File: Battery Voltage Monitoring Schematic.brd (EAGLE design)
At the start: 82.2 x 68.6 mm, 44 parts, among them IC1 74HC595D, J1 22-27-2031-03, U1 INA3221., U2 INA3221., X1 22-27-2021-02, X3 2516-

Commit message: Add files via upload
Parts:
- removed PAD10_M1, PAD11_GND, PAD12_M2, PAD13_GND, PAD14_M3, PAD15_GND, PAD16_M4, PAD1_GND, PAD2_B1, PAD3_GND, PAD4_B2, PAD5_GND, PAD6_B3, PAD7_GND, PAD8_B4, PAD9_GND: 3,81/1,9, Moira:3,81/1,9
- removed X1: 22-27-2021-02, con-molex:6410-02
- added U$1, U$2, U$3, U$4, U$5, U$6, U$7, U$8: MKDS_5/2-6,352, Moira:MKDS_5/2-6,35
- added U$10: ARVP_LOGO, ARVP:ARVP
- added U$9: ARVP_MOLEX_FEMALE, ARVP_MOLEX_FEMALE:ARVP_MOLEX_FEMALE
- moved R4 40.9 mm to (36.8, 74.9), turned to 180 degrees
- moved R7 25.9 mm to (36.8, 36.8), turned to 180 degrees
- moved R1 21.7 mm to (36.8, 62.2), turned to 180 degrees
- moved R3 11.7 mm to (36.8, 49.5), turned to 180 degrees
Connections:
- net +5V: now also U$9.P$1; no longer X1.1
- net 0-26V_BATTERY1: now also U$1.1; no longer PAD2_B1.1
- net 0-26V_BATTERY2: now also U$2.1; no longer PAD4_B2.1
- net 0-26V_BATTERY3: now also U$3.1; no longer PAD6_B3.1
- net 0-26V_BATTERY4: now also U$4.1; no longer PAD8_B4.1
- net AGND: now also U$1.2, U$2.2, U$3.2, U$4.2, U$5.2, U$6.2, U$7.2, U$8.2; no longer PAD11_GND.1, PAD13_GND.1, PAD15_GND.1, PAD1_GND.1, PAD3_GND.1, PAD5_GND.1, PAD7_GND.1, PAD9_GND.1
- net GND: now also U$9.P$2; no longer X1.2
- net MOTOR1: now also U$5.1; no longer PAD10_M1.1
- net MOTOR2: now also U$6.1; no longer PAD12_M2.1
- net MOTOR3: now also U$7.1; no longer PAD14_M3.1
- net MOTOR4: now also U$8.1; no longer PAD16_M4.1
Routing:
- net 0-26V_BATTERY1: track 90.3 -> 141.5 mm, vias 2 -> 3
- net 0-26V_BATTERY3: track 96.6 -> 131.2 mm
- net 0-26V_BATTERY2: track 87.2 -> 116.2 mm, vias 0 -> 2
- net MOTOR1: track 119.1 -> 90.6 mm, vias 2 -> 1
- net MOTOR2: track 103.5 -> 87.2 mm, vias 4 -> 3
- net AGND: track 46.6 -> 32.3 mm
- net 0-26V_BATTERY4: track 90.6 -> 100.4 mm
- net MOTOR3: track 86.0 -> 78.7 mm, vias 1 -> 0
- net MOTOR4: track 62.8 -> 69.2 mm, vias 3 -> 2
- net +5V: track 74.6 -> 70.9 mm
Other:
- board size 82.2 x 68.6 mm -> 82.2 x 88.9 mm
- board text added: "ARVP BATTERY VOLTAGE MONITORING"
- board text added: "M. Blenkinsopp"
- board text added: "REV 1.1 07/2017"

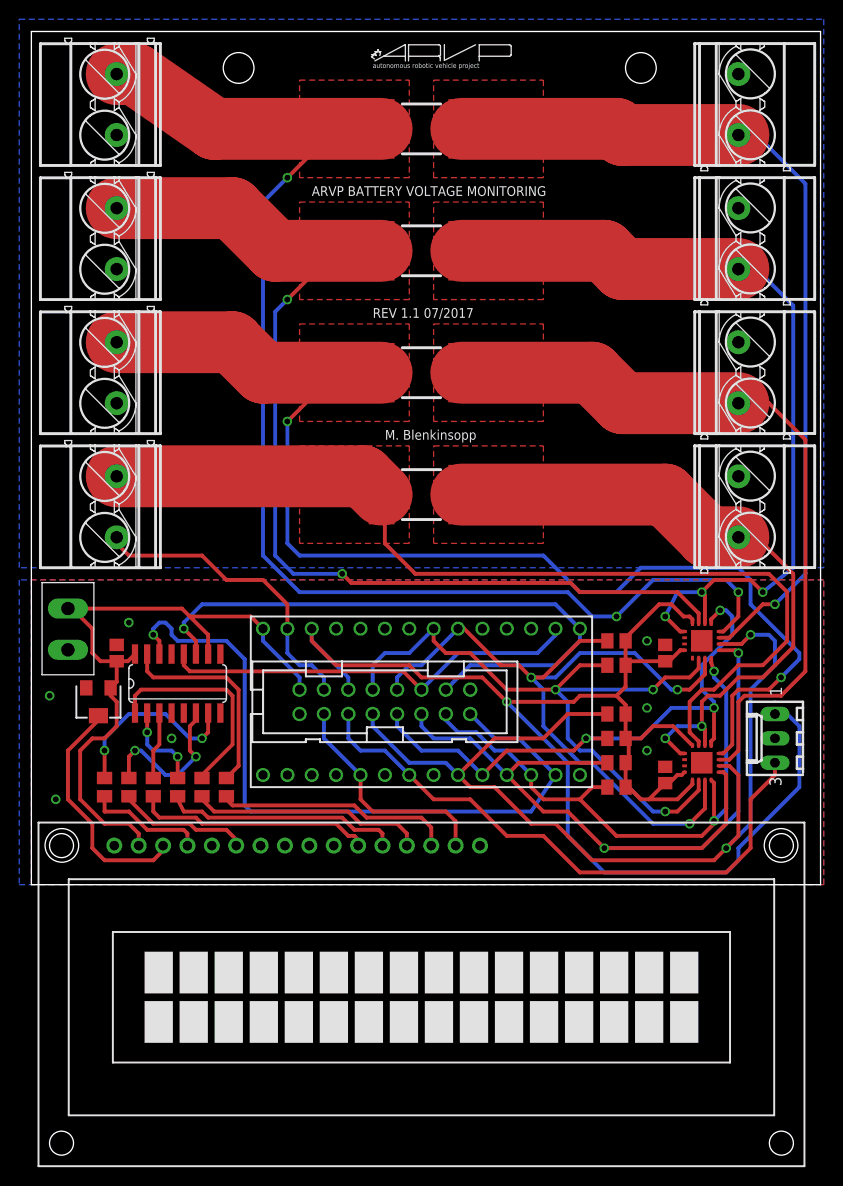
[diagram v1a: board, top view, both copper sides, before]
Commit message: Add files via upload
Battery AGND connected to teensy GND
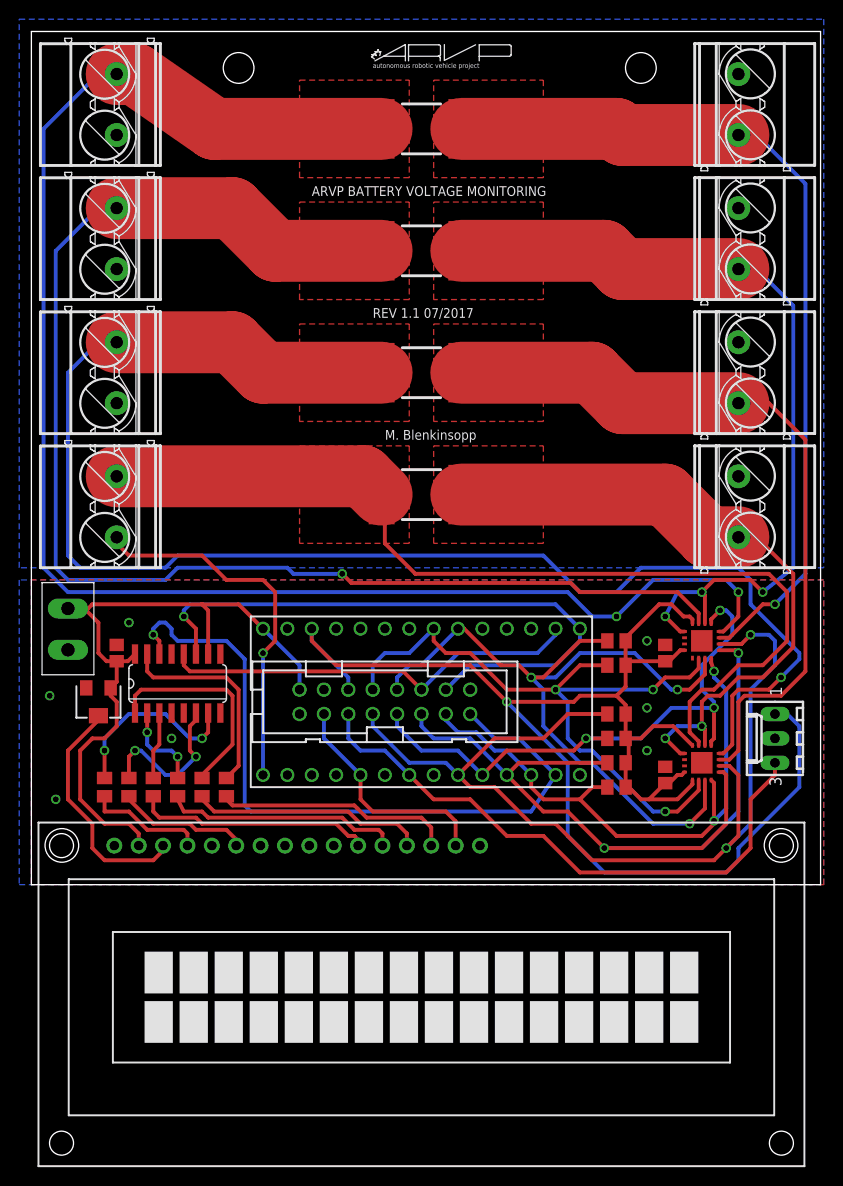
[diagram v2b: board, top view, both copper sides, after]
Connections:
- net AGND: no longer U$4.2
- net GND: now also U$4.2
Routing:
- net GND: track 0.27 -> 39.1 mm, vias 7 -> 8
- net AGND: track 32.3 -> 0.00 mm
- net 0-26V_BATTERY1: track 141.5 -> 167.2 mm, vias 3 -> 2
- net 0-26V_BATTERY2: track 116.2 -> 141.7 mm, vias 2 -> 1
- net 0-26V_BATTERY3: track 131.2 -> 155.5 mm, vias 2 -> 1
- net LCD(SCK): track 64.3 -> 65.0 mm

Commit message: Changed terminal block layout; Modified some routing; Fixed DRC issues
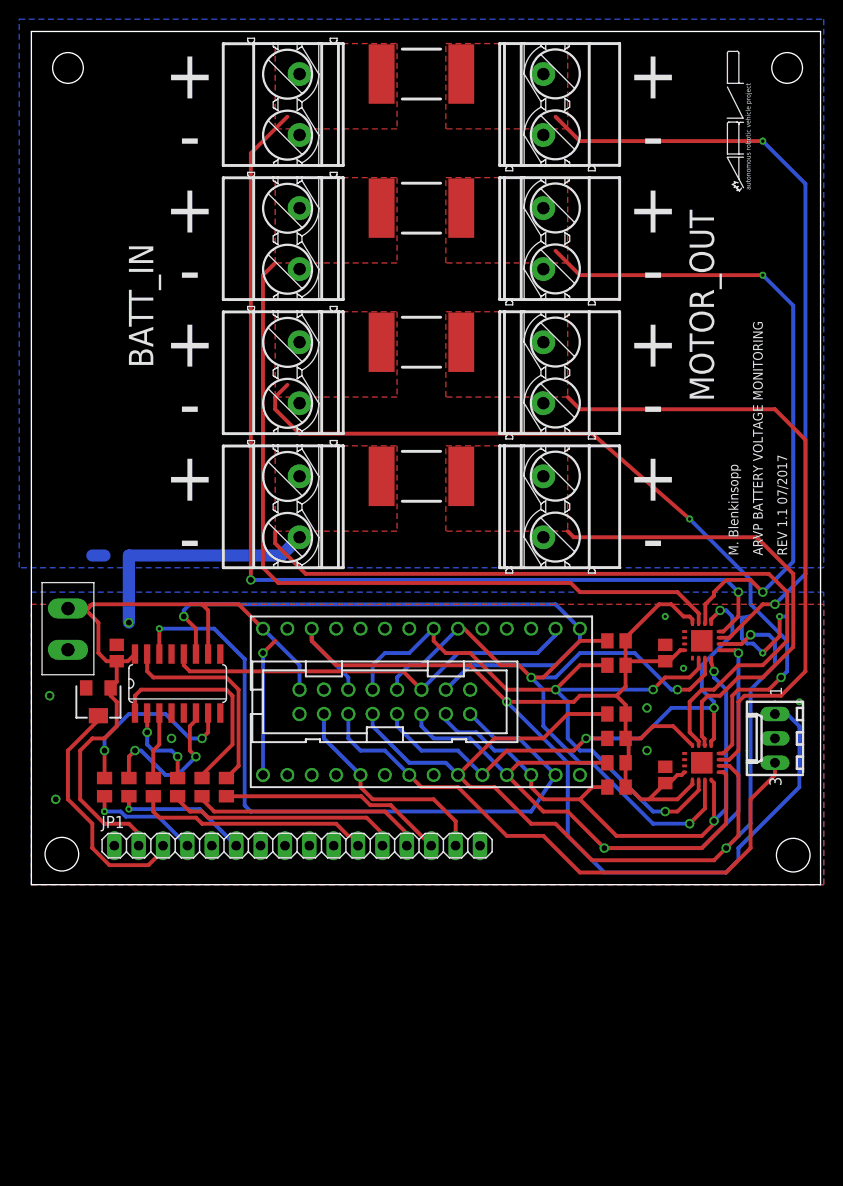
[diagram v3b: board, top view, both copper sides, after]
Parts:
- removed DIS1: TUXGR_16X2_R2, display-lcd:TUXGR_16X2_R2
- removed U$8: MKDS_5/2-6,352, Moira:MKDS_5/2-6,35
- added JP1: (no value), pinhead:1X16
- added U$11: MKDS_5/2-6,352, Moira:MKDS_5/2-6,35
- moved U$10 41.4 mm to (71.1, 68.6), turned to 90 degrees
- moved U$5 34.5 mm to (49.5, 49.5)
- moved U$7 34.5 mm to (49.5, 77.5)
- moved U$6 20.3 mm to (49.5, 63.5)
- moved U$1 19.0 mm to (24.1, 77.5)
- moved U$2 19.0 mm to (24.1, 63.5)
- moved U$3 19.0 mm to (24.1, 49.5)
- moved U$4 19.0 mm to (24.1, 35.6)
- moved R4 5.71 mm to (36.8, 80.6)
- moved R1 4.45 mm to (36.8, 66.7)
- moved R3 3.17 mm to (36.8, 52.7)
- moved R7 1.91 mm to (36.8, 38.7)
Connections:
- net +5V: now also JP1.2; no longer DIS1.2
- net AGND: no longer U$1.2, U$2.2, U$3.2, U$5.2, U$6.2, U$7.2, U$8.2
- net BACKLIGHT: now also JP1.15; no longer DIS1.15
- net ENABLE: now also JP1.6; no longer DIS1.6
- net GND: now also JP1.1, JP1.16, JP1.5, U$1.2, U$11.1, U$2.2, U$3.2, U$5.1, U$6.1, U$7.1; no longer DIS1.1, DIS1.16, DIS1.5
- net LCD_DB4: now also JP1.11; no longer DIS1.11
- net LCD_DB5: now also JP1.12; no longer DIS1.12
- net LCD_DB6: now also JP1.13; no longer DIS1.13
- net LCD_DB7: now also JP1.14; no longer DIS1.14
- net MOTOR1: now also U$7.2; no longer U$5.1
- net MOTOR2: now also U$6.2; no longer U$6.1, U1.1
- net MOTOR3: now also U$5.2; no longer U$7.1
- net MOTOR4: now also U$11.2; no longer U$8.1, U2.1
- net N$18: now also JP1.3; no longer DIS1.3
- net RS: now also JP1.4; no longer DIS1.4
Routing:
- net 0-26V_BATTERY3: track 155.5 -> 84.3 mm, vias 1 -> 2
- net 0-26V_BATTERY1: track 167.2 -> 106.4 mm
- net 0-26V_BATTERY2: track 141.7 -> 81.3 mm, vias 1 -> 0
- net 0-26V_BATTERY4: track 100.4 -> 79.5 mm
- net MOTOR4: track 69.2 -> 49.5 mm, vias 2 -> 0
- net MOTOR2: track 87.2 -> 68.1 mm, vias 3 -> 2
- net GND: track 39.1 -> 52.7 mm, vias 8 -> 12
- net MOTOR3: track 78.7 -> 66.5 mm
- net MOTOR1: track 90.6 -> 81.3 mm, vias 1 -> 2
- net DATA: track 76.1 -> 74.3 mm
- net LCD_DB7: track 24.8 -> 23.5 mm
- net RS: track 12.4 -> 11.7 mm, vias 0 -> 1
- net BACKLIGHT: track 23.9 -> 23.1 mm
- net ENABLE: track 13.9 -> 14.1 mm, vias 0 -> 1
- removed copper zone on layer 16, net AGND
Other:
- board text added: "+"
- board text added: "-"
- board text added: "BATT_IN"
- board text added: "MOTOR_OUT"

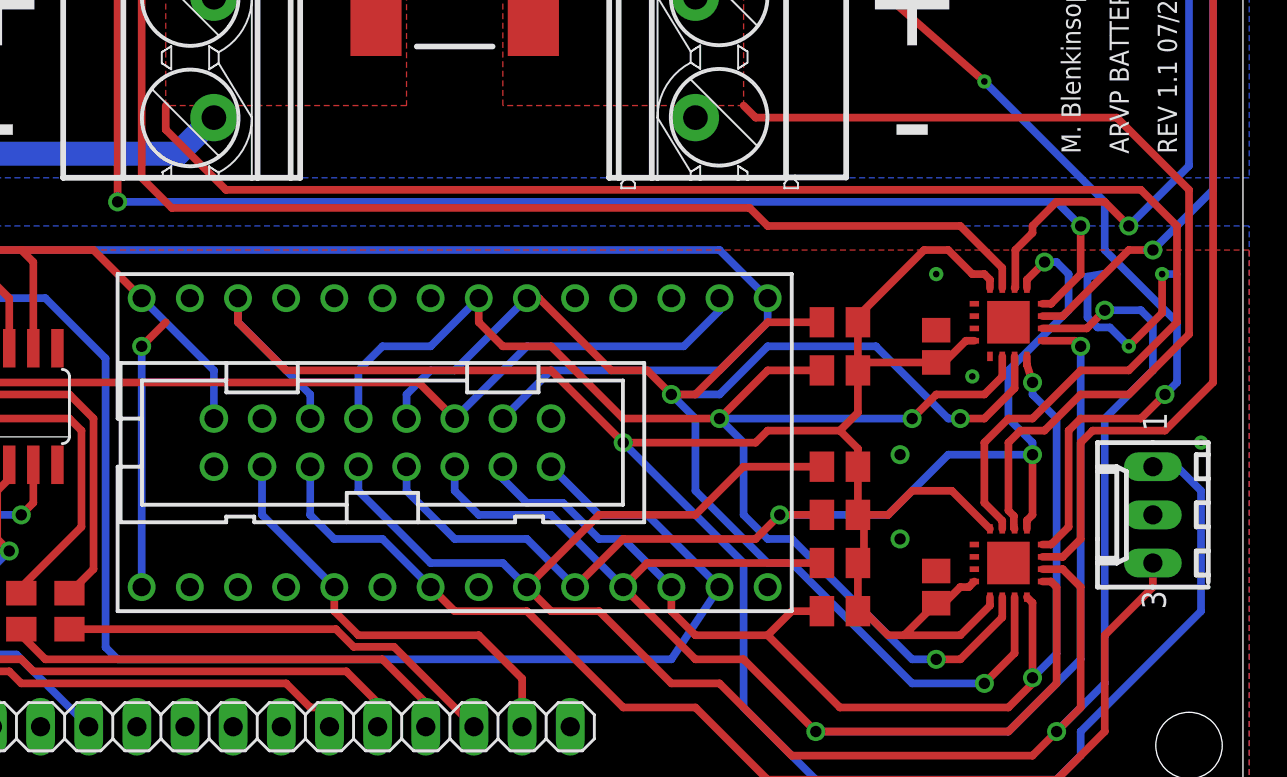
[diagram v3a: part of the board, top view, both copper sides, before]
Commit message: Change position of 2 vias
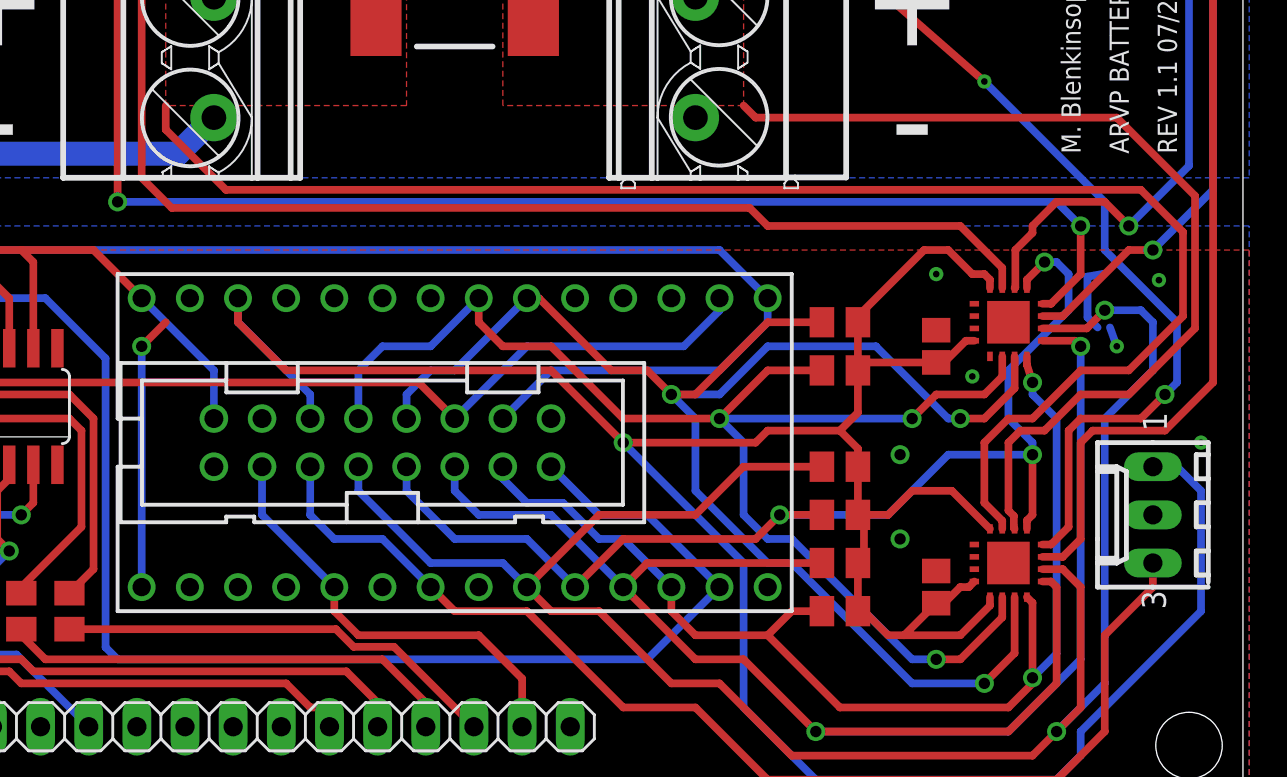
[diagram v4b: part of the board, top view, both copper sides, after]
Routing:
- net GND: track 52.7 -> 46.4 mm
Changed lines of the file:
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@@
 <vertex x="21.59" y="41.91"/>
 </polygon>
-<wire x1="74.93" y1="21.59" x2="72.39" y2="19.05" width="0.4064" layer="1"/>
+<wire x1="75.2475" y1="21.9075" x2="72.39" y2="19.05" width="0.4064" layer="1"/>
 <wire x1="72.39" y1="19.05" x2="69.85" y2="19.05" width="0.4064" layer="1"/>
 <wire x1="69.85" y1="19.05" x2="67.31" y2="16.51" width="0.4064" layer="1"/>
@@
 <wire x1="65.715" y1="11.12" x2="65.715" y2="10.69" width="0.4064" layer="1"/>
 <contactref element="U$4" pad="1"/>
-<wire x1="74.93" y1="21.59" x2="74.93" y2="26.67" width="0.4064" layer="1"/>
-<wire x1="73.025" y1="28.575" x2="74.93" y2="26.67" width="0.4064" layer="1"/>
+<wire x1="75.2475" y1="21.9075" x2="75.2475" y2="26.3525" width="0.4064" layer="1"/>
+<wire x1="73.025" y1="28.575" x2="75.2475" y2="26.3525" width="0.4064" layer="1"/>
 <wire x1="21.59" y1="31.75" x2="24.765" y2="28.575" width="0.4064" layer="1"/>
 <wire x1="21.59" y1="31.75" x2="21.59" y2="33.02" width="0.4064" layer="1"/>
@@
 <wire x1="18.415" y1="4.445" x2="18.415" y2="19.685" width="0.4064" layer="16"/>
 <wire x1="18.415" y1="4.445" x2="19.05" y2="3.81" width="0.4064" layer="16"/>
-<wire x1="19.05" y1="3.81" x2="48.26" y2="3.81" width="0.4064" layer="16"/>
-<wire x1="48.26" y1="3.81" x2="50.8" y2="7.62" width="0.4064" layer="16"/>
+<wire x1="19.05" y1="3.81" x2="46.99" y2="3.81" width="0.4064" layer="16"/>
+<wire x1="46.99" y1="3.81" x2="50.8" y2="7.62" width="0.4064" layer="16"/>
 <contactref element="X3" pad="15"/>
 <wire x1="50.8" y1="7.62" x2="46.99" y2="11.43" width="0.4064" layer="16"/>
@@
 <wire x1="67.945" y1="15.875" x2="69.85" y2="17.78" width="0.4064" layer="1"/>
 <wire x1="69.85" y1="17.78" x2="72.39" y2="17.78" width="0.4064" layer="1"/>
-<wire x1="72.39" y1="17.78" x2="75.565" y2="20.955" width="0.4064" layer="1"/>
-<wire x1="75.565" y1="20.955" x2="75.565" y2="28.575" width="0.4064" layer="1"/>
-<wire x1="75.565" y1="28.575" x2="71.755" y2="32.385" width="0.4064" layer="1"/>
+<wire x1="72.39" y1="17.78" x2="75.8825" y2="21.2725" width="0.4064" layer="1"/>
+<wire x1="75.8825" y1="21.2725" x2="75.8825" y2="28.2575" width="0.4064" layer="1"/>
+<wire x1="75.8825" y1="28.2575" x2="71.755" y2="32.385" width="0.4064" layer="1"/>
 <contactref element="U$11" pad="2"/>
 <wire x1="71.755" y1="32.385" x2="52.705" y2="32.385" width="0.4064" layer="1"/>
@@
 <via x="76.2" y="15.24" extent="1-16" drill="0.35"/>
 <wire x1="70.2104" y1="21.84823125" x2="70.74323125" y2="21.3154" width="0.4064" layer="16"/>
-<wire x1="70.74323125" y1="21.3154" x2="71.3946" y2="21.3154" width="0.4064" layer="16"/>
-<wire x1="71.3946" y1="21.3154" x2="72.39" y2="20.32" width="0.4064" layer="16"/>
+<wire x1="71.3946" y1="21.3154" x2="71.755" y2="20.32" width="0.4064" layer="16"/>
 <wire x1="71.07250625" y1="24.1506" x2="70.2104" y2="23.99670625" width="0.4064" layer="16"/>
 <wire x1="70.2104" y1="23.99670625" x2="70.2104" y2="21.84823125" width="0.4064" layer="16"/>
-<via x="72.39" y="20.32" extent="1-16" drill="0.35"/>
-<wire x1="72.39" y1="20.32" x2="74.1454" y2="22.0754" width="0.4064" layer="1"/>
-<wire x1="74.1454" y1="22.0754" x2="74.1454" y2="24.13" width="0.4064" layer="1"/>
-<via x="74.1454" y="24.13" extent="1-16" drill="0.35"/>
-<wire x1="74.1454" y1="24.13" x2="74.93" y2="24.13" width="0.4064" layer="16"/>
+<via x="71.755" y="20.32" extent="1-16" drill="0.35"/>
+<via x="73.9775" y="23.8125" extent="1-16" drill="0.35"/>
 <contactref element="JP1" pad="1"/>
 <contactref element="JP1" pad="16"/>
